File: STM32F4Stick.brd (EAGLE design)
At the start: 44.5 x 23.4 mm, 36 parts, among them U1 MIC5219 3.3V

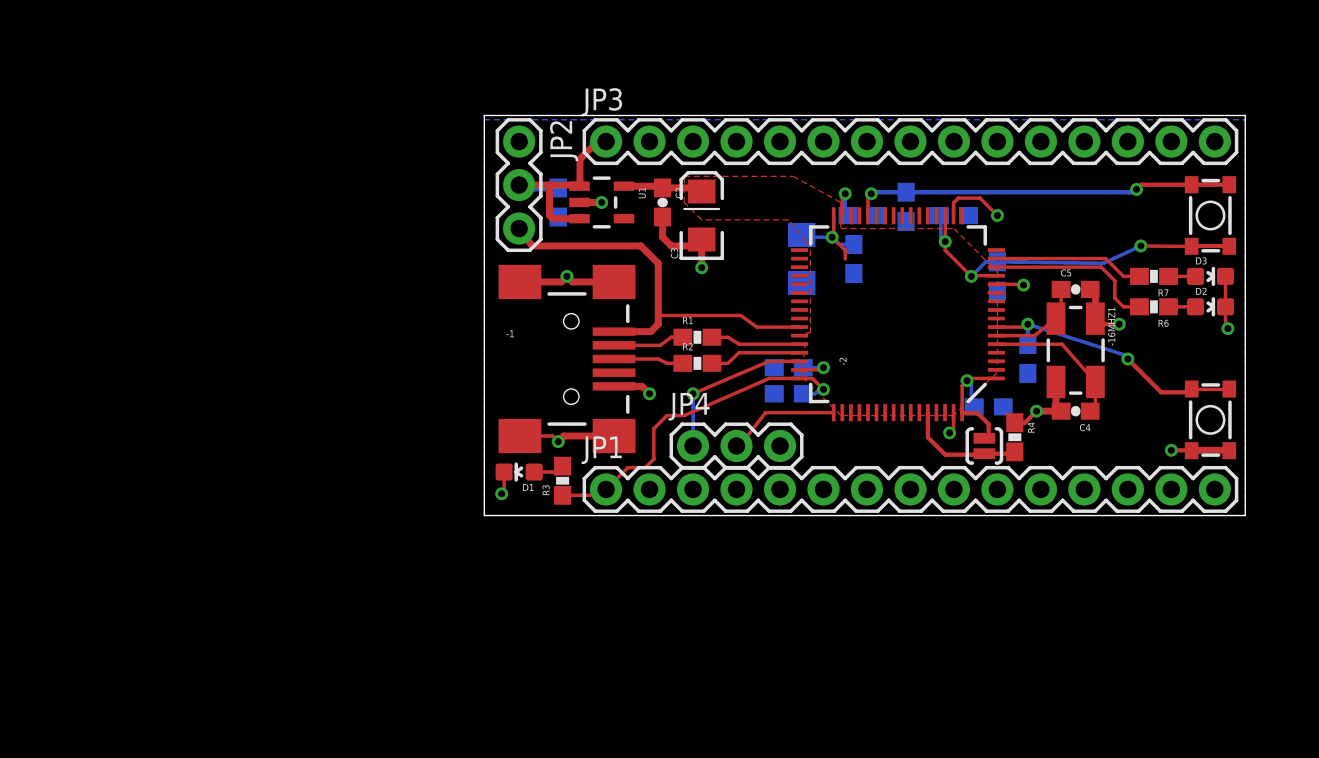
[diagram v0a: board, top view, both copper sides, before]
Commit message: Extension header additions to schematic. Routing is complete on the board. The second extension header connections needs to be added.
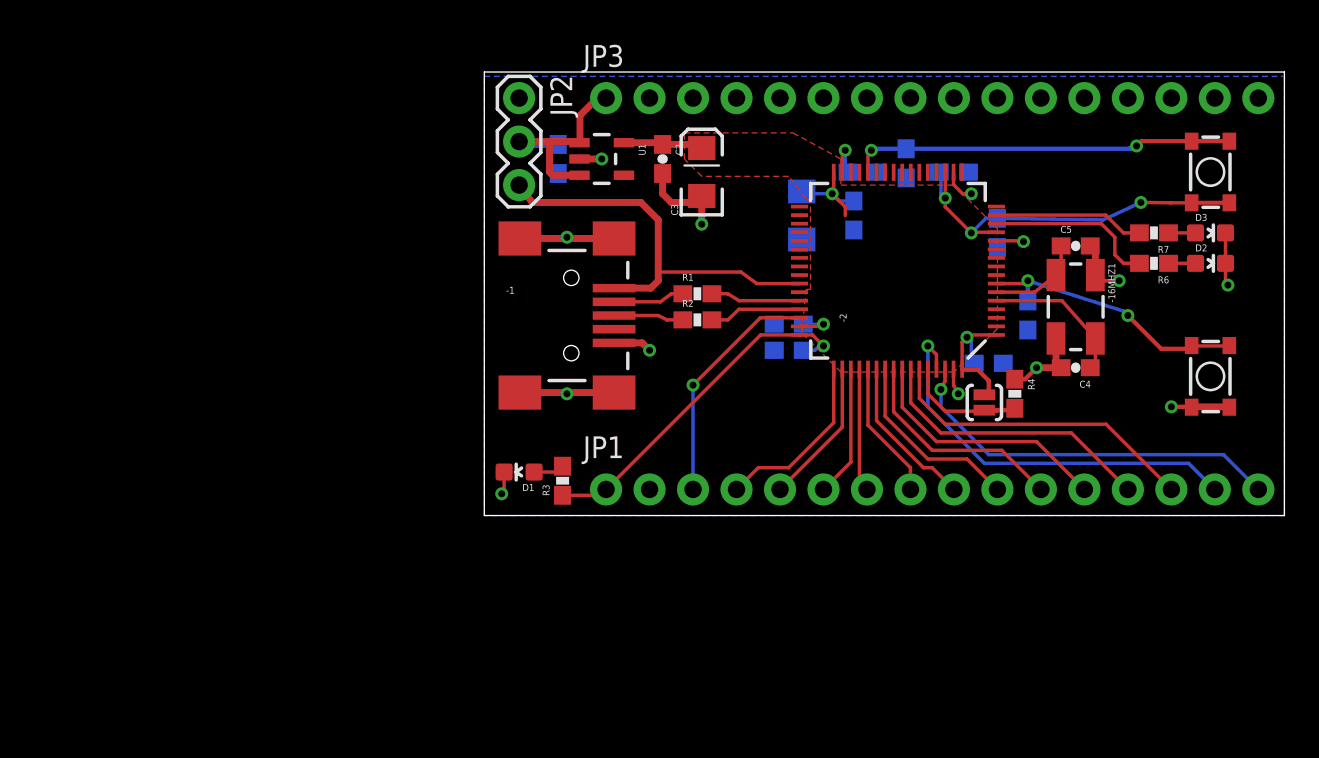
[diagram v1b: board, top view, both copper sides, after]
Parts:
- removed JP4: (no value), SparkFun-Connectors:1X03
- JP1, JP3: value M15 -> M161X16_NO_SILK; device SparkFun-Connectors:1X15 -> SparkFun-Connectors:1X16_NO_SILK
- moved R5 2.54 mm to (24.6, 20.6)
- moved -16MHZ1 2.54 mm to (34.5, 12.2)
- moved -2 2.54 mm to (24.2, 14.3)
- moved C10 2.54 mm to (30.0, 16.5)
- moved C11 2.54 mm to (29.5, 8.89)
- moved C13 2.54 mm to (17.8, 11.2)
- moved D3 2.54 mm to (42.4, 16.5)
- moved R1 2.54 mm to (12.4, 13.0)
- moved R7 2.54 mm to (39.1, 16.5)
- moved R4 2.54 mm to (31.0, 7.11)
- moved S1 2.54 mm to (42.4, 8.13)
- moved SJ1 2.54 mm to (29.2, 6.60)
- moved -1 2.54 mm to (5.08, 11.7)
- moved C1 2.54 mm to (4.32, 20.8)
- moved C12 2.54 mm to (18.5, 17.5)
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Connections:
- removed net N$11: JP1.9
- removed net N$12: JP1.8
- removed net N$13: JP1.7
- removed net N$14: JP1.6
- removed net N$15: JP1.5
- removed net N$16: JP1.4
- removed net N$17: JP1.3
- removed net N$2: JP1.15
- removed net N$5: JP1.14
- removed net N$6: JP1.13
- removed net N$7: JP1.12
- removed net N$8: JP1.11
- removed net N$9: JP1.10
- new net P50: -2.50, JP1.5
- new net P51: -2.51, JP1.6
- new net P52: -2.52, JP1.7
- new net P53: -2.53, JP1.8
- new net P54: -2.54, JP1.9
- new net P55: -2.55, JP1.10
- new net P56: -2.56, JP1.11
- new net P57: -2.57, JP1.12
- new net P58: -2.58, JP1.13
- new net P59: -2.59, JP1.14
- new net P61: -2.61, JP1.15
- new net P62: -2.62, JP1.16
- new net USB_ID: -2.43
- net GND: no longer JP4.3
- net SWDCK: now also JP1.4; no longer JP4.2
- net SWDIO: now also JP1.3; no longer JP4.1
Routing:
- net P61: track 0.00 -> 23.9 mm, vias 0 -> 1
- net P62: track 0.00 -> 22.8 mm, vias 0 -> 1
- net P59: track 0.00 -> 18.6 mm
- net P58: track 0.00 -> 16.7 mm
- net P57: track 0.00 -> 14.9 mm
- net P56: track 0.00 -> 13.0 mm
- net P55: track 0.00 -> 11.1 mm
- net P54: track 0.00 -> 9.19 mm
- net P50: track 0.00 -> 8.53 mm
- net P53: track 0.00 -> 8.05 mm
- net P51: track 0.00 -> 7.69 mm
- net P52: track 0.00 -> 7.21 mm
- net SWDIO: track 9.66 -> 13.9 mm
- net SWDCK: track 7.02 -> 10.4 mm
- net GND: track 43.8 -> 41.9 mm
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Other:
- board size 44.5 x 23.4 mm -> 46.7 x 25.9 mm

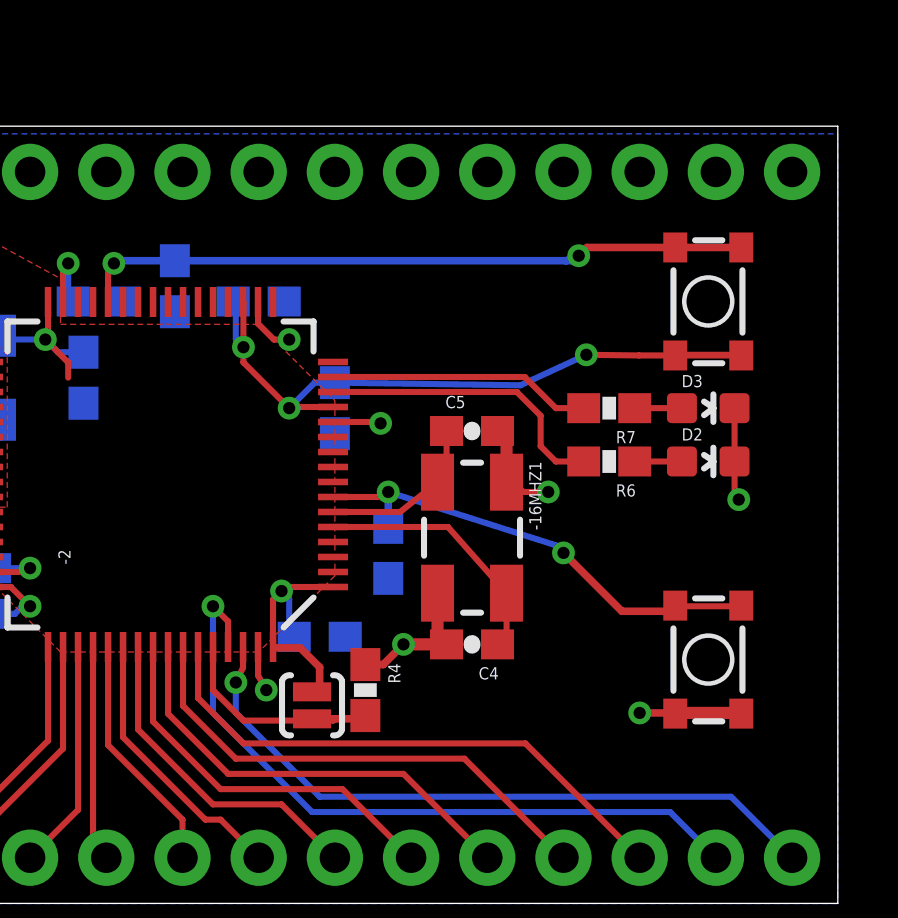
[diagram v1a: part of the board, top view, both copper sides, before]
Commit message: Added SD-Card. Still need to route the extension pins.
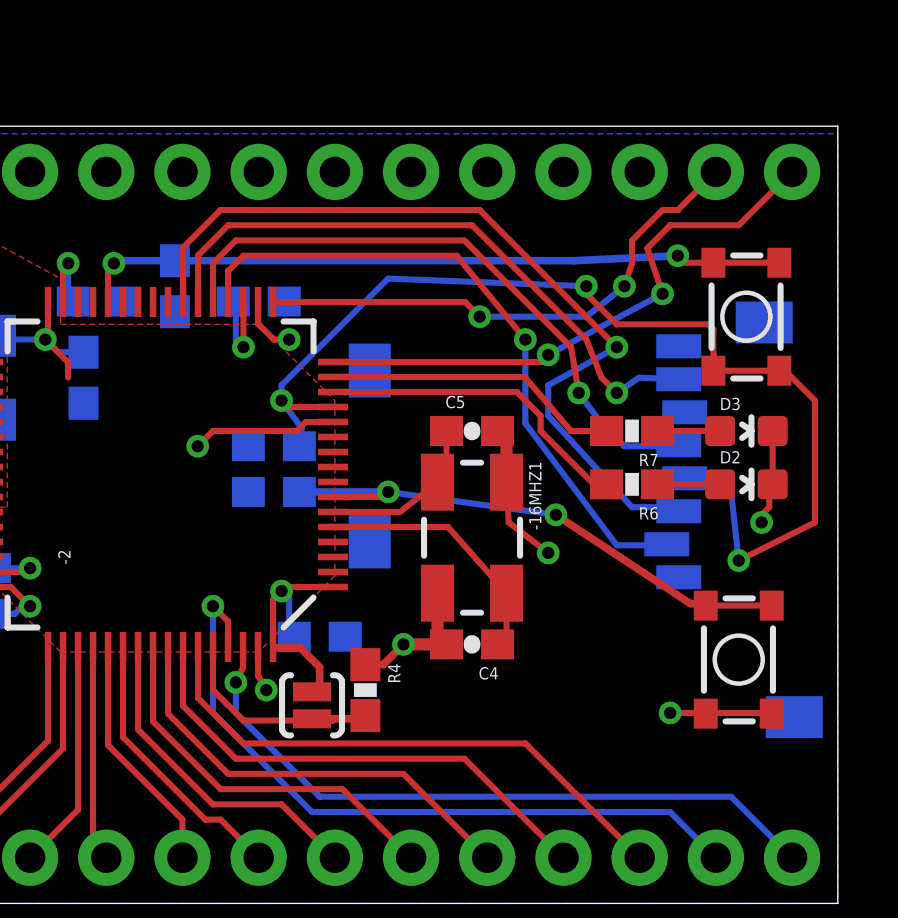
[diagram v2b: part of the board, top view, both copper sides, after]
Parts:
- added U2: USD-SOCKETNEW, SparkFun-Connectors:MICRO-SD-SOCKET-PP
- moved C14 4.32 mm to (27.9, 13.7), turned to 0 degrees
- moved C10 2.40 mm to (27.9, 15.2), turned to 0 degrees
- moved D3 1.48 mm to (43.7, 15.7)
- moved D2 1.48 mm to (43.7, 14.0)
- moved S2 1.37 mm to (43.7, 19.6)
- moved R7 1.08 mm to (39.9, 15.7)
- moved R6 1.08 mm to (39.9, 14.0)
- moved S1 1.02 mm to (43.4, 8.13)
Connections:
- removed net N$20: JP3.15
- new net P16: -2.16, JP3.16
- new net P17: -2.17, JP3.15
- new net SD_CS: -2.20, U2.2
- new net SD_MISO: -2.22, U2.7
- new net SD_MOSI: -2.23, U2.3
- new net SD_SCK: -2.21, U2.5
- net GND: now also U2.6, U2.GND1, U2.GND3
- net VCC: now also U2.4
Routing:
- net SD_MOSI: track 0.00 -> 28.1 mm, vias 0 -> 1
- net SD_CS: track 0.00 -> 22.0 mm, vias 0 -> 1
- net SD_MISO: track 0.00 -> 20.8 mm, vias 0 -> 1
- net SD_SCK: track 0.00 -> 20.7 mm, vias 0 -> 1
- net P16: track 0.00 -> 19.1 mm, vias 0 -> 2
- net P17: track 0.00 -> 17.6 mm, vias 0 -> 2
- net VCC: track 65.3 -> 80.9 mm, vias 6 -> 7
- net GND: track 41.9 -> 47.0 mm
- net NRST: track 16.3 -> 18.6 mm
- net LED_RED: track 8.79 -> 9.94 mm
- net BOOT1: track 23.2 -> 24.0 mm
- net LED_BLUE: track 9.91 -> 10.7 mm
- net N$19: track 1.57 -> 2.08 mm
- net N$18: track 1.57 -> 2.08 mm

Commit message: Finished Schematic / Board layout. Silkscreen needs to be added
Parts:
- removed -16MHZ1: CRYSTAL-GROUNDED, SparkFun-FreqCtrl:CRYSTAL-SMD-5X3
- added Q1: (no value), adafruit:NX3225
- added R10, R11, R8, R9: 100k, SparkFun-Resistors:0603-RES
- moved C7 2.27 mm to (20.6, 15.5)
- moved C3 1.80 mm to (14.5, 19.8), flipped to the bottom
- moved C2 1.52 mm to (11.9, 20.8), flipped to the bottom
- moved C5 1.37 mm to (34.0, 14.5)
- moved R5 1.02 mm to (24.6, 19.6)
- moved U2 1.02 mm to (30.7, 18.8)
- moved C11 1.02 mm to (29.5, 7.87)
- moved -2 1.02 mm to (24.2, 13.3)
- moved C10 1.02 mm to (27.9, 14.2)
- moved C13 1.02 mm to (17.8, 10.2)
- moved C14 1.02 mm to (27.9, 12.7)
- moved C9 1.02 mm to (17.8, 8.64)
- moved D3 1.02 mm to (43.7, 14.7)
- moved R4 1.02 mm to (31.0, 6.10)
- moved R7 1.02 mm to (39.9, 14.7)
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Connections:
- removed net N$21: JP3.14
- removed net N$22: JP3.13
- removed net N$23: JP3.12
- removed net N$24: JP3.11
- removed net N$25: JP3.10
- removed net N$26: JP3.9
- removed net N$27: JP3.8
- removed net N$28: JP3.7
- removed net N$29: JP3.6
- removed net N$30: JP3.5
- removed net N$31: JP3.4
- removed net N$32: JP3.3
- new net P26: -2.26, JP3.14
- new net P27: -2.27, JP3.13
- new net P29: -2.29, JP3.12
- new net P30: -2.30, JP3.11, R9.1
- new net P33: -2.33, JP3.10
- new net P34: -2.34, JP3.9
- new net P35: -2.35, JP3.8
- new net P36: -2.36, JP3.7
- new net P37: -2.37, JP3.6
- new net P39: -2.39, JP3.5
- new net P40: -2.40, JP3.4
- new net P41: -2.41, JP3.3
- net GND: now also Q1.2, Q1.4; no longer -16MHZ1.2, -16MHZ1.4
- net N$3: now also Q1.1; no longer -16MHZ1.3
- net N$4: now also Q1.3; no longer -16MHZ1.1
- net P52: now also R10.1
- net P57: now also R11.1
- net USB_ID: now also R8.1
- net VCC: now also R10.2, R11.2, R8.2, R9.2
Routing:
- net P30: track 0.00 -> 21.9 mm, vias 0 -> 2
- net P26: track 0.00 -> 19.9 mm
- net P27: track 0.00 -> 18.5 mm
- net VCC: track 80.9 -> 98.9 mm, vias 7 -> 9
- net P29: track 0.00 -> 16.7 mm, vias 0 -> 1
- net P33: track 0.00 -> 16.2 mm, vias 0 -> 1
- net P34: track 0.00 -> 15.2 mm
- net P41: track 0.00 -> 14.9 mm
- net P35: track 0.00 -> 14.2 mm
- net P36: track 0.00 -> 13.4 mm
- net P40: track 0.00 -> 13.2 mm
- net P39: track 0.00 -> 12.8 mm
- net P37: track 0.00 -> 12.8 mm
- net GND: track 47.0 -> 41.4 mm, vias 13 -> 18
- net USB_ID: track 0.00 -> 3.18 mm, vias 0 -> 1
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- added copper zone on layer 1, net GND

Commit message: Final version for Rev A.
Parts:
- added C15: 0.1uF, SparkFun-Capacitors:0603-CAP
- added LOGO1: OSHW-LOGOM, SparkFun-Aesthetics:OSHW-LOGO-M
- C5: value 12pF -> 2.2uF
- C6: value 2.2uF -> 12pF
- JP2: device SparkFun-Connectors:1X03 -> SparkFun-Connectors:1X03_NO_SILK
- R10, R11: value 100k -> 1K
- R4, R5: value 10K -> 100k
- R6, R7: value 1K -> 100k
- R8, R9: value 100k -> 10K
- moved R7 21.2 mm to (21.8, 3.56), flipped to the bottom, turned to 0 degrees
- moved R10 20.5 mm to (39.9, 13.2), flipped to the top, turned to 180 degrees
- moved R11 20.5 mm to (39.9, 14.7), flipped to the top, turned to 180 degrees
- moved R6 19.8 mm to (21.8, 5.08), flipped to the bottom, turned to 0 degrees
- moved R5 14.4 mm to (38.9, 21.6), turned to 180 degrees
- moved R9 14.4 mm to (24.6, 19.6), turned to 90 degrees
- moved C5 12.8 mm to (22.1, 19.1), flipped to the bottom, turned to 180 degrees
- moved C6 12.8 mm to (34.0, 14.5), flipped to the top, turned to 0 degrees
- moved R4 10.7 mm to (21.1, 10.2), flipped to the bottom
- moved R8 10.7 mm to (31.0, 6.10), flipped to the top
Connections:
- new net N$2: C15.1, U1.4
- net BOOT0: now also R8.2; no longer R4.2
- net BOOT1: now also R9.2; no longer R5.2
- net GND: now also C15.2, R8.1, R9.1; no longer R4.1, R5.1
- net LED_BLUE: now also R10.2; no longer R6.2
- net LED_RED: now also R11.2; no longer R7.2
- net N$1: now also C5.1; no longer C6.1
- net N$18: now also R10.1; no longer R6.1
- net N$19: now also R11.1; no longer R7.1
- net N$4: now also C6.1; no longer C5.1
- net P30: now also R5.1; no longer R9.1
- net P52: now also R7.1; no longer R10.1
- net P57: now also R6.1; no longer R11.1
- net USB_ID: now also R4.1; no longer R8.1
- net VCC: now also R4.2, R5.2, R6.2, R7.2; no longer R10.2, R11.2, R8.2, R9.2
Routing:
- net N$2: track 0.00 -> 2.36 mm
- net GND: track 41.4 -> 40.9 mm
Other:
- board text added: "100k"
- board text added: "3V3"
- board text added: "5V"
- board text added: "A13"
- board text added: "A14"
- board text added: "A15"
- board text added: "A2"
- board text added: "A3"
- board text added: "A8"
- board text added: "B0"
- board text added: "B1"
- board text added: "B10"
- board text added: "B11"
- board text added: "B12"
- board text added: "B13"
- board text added: "B14"
- board text added: "B15"
- board text added: "B3"
- board text added: "B4"
- board text added: "B5"
- board text added: "B6"
- board text added: "B7"
- board text added: "B8"
- board text added: "B9"
- board text added: "BOOT0"
- board text added: "BOOT1/PB2"
- board text added: "BTN"
- board text added: "C10"
- board text added: "C11"
- board text added: "C12"
- board text added: "C6"
- board text added: "C8"
- board text added: "C9"
- board text added: "D2"
- board text added: "FURKAN CAYCI"
- board text added: "GND"
- board text added: "JTCK"
- board text added: "JTD0"
- board text added: "JTDI"
- board text added: "JTMS"
- board text added: "JUNE 2014"
- board text added: "LED1"
- board text added: "LED2"
- board text added: "MISO"
- board text added: "MOSI"
- board text added: "NJTRST"
- board text added: "NSS"
- board text added: "PA0"
- board text added: "PA1"
- board text added: "POWER"
- board text added: "RESET"
- board text added: "REV A"
- board text added: "RX UART2 TX"
- board text added: "SCK"
- board text added: "SCL I2C3 SDA"
- board text added: "SD/MMC CARD (SPI MODE) SPI1 A4,5,6,7"
- board text added: "SDA I2C2 SCL"
- board text added: "SPI2"
- board text added: "STM32F4Stick"
- board text added: "SWCLK"
- board text added: "SWD"
- board text added: "SWDIO"
- board text added: "USB"
- board text added: "USB ID Pull high"
- board text added: "https://github.com/fcayci/STM32F4Stick"

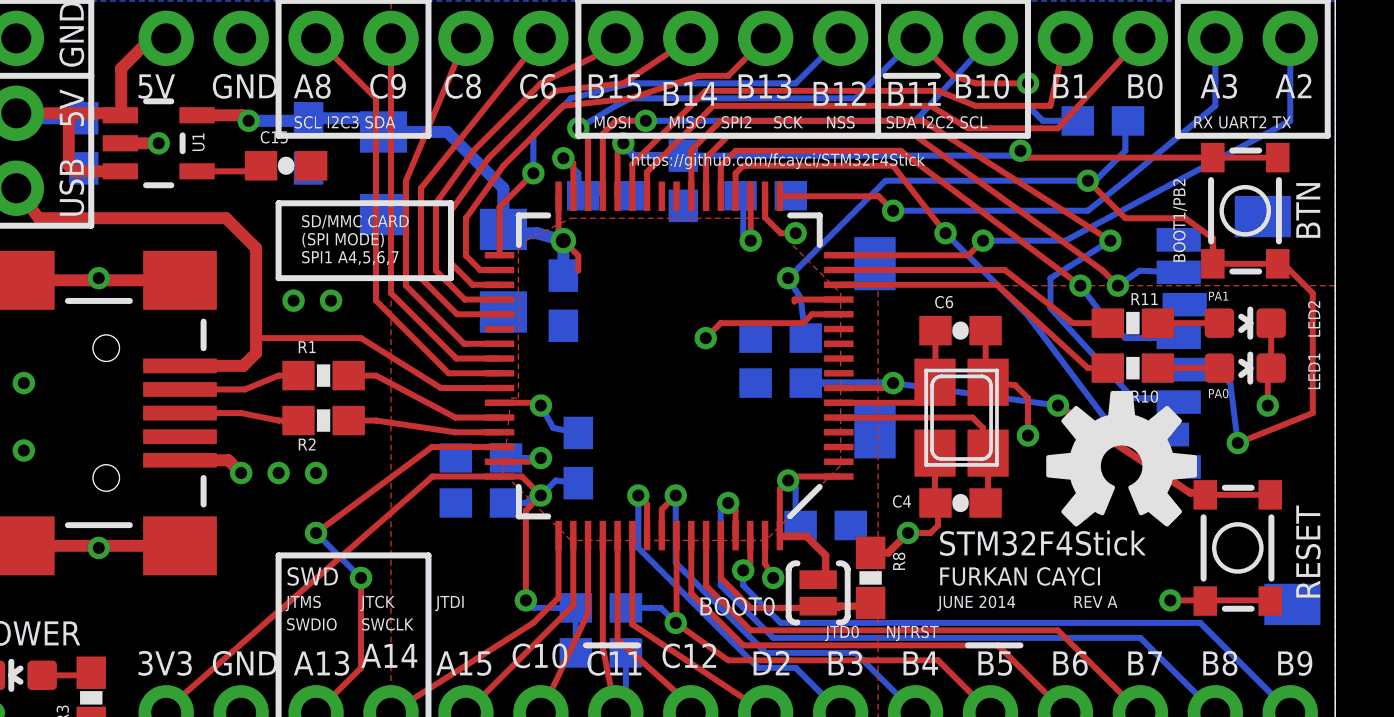
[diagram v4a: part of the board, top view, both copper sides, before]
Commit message: Small fixes to the usb resistors and a component might get in the way of SD card slot.
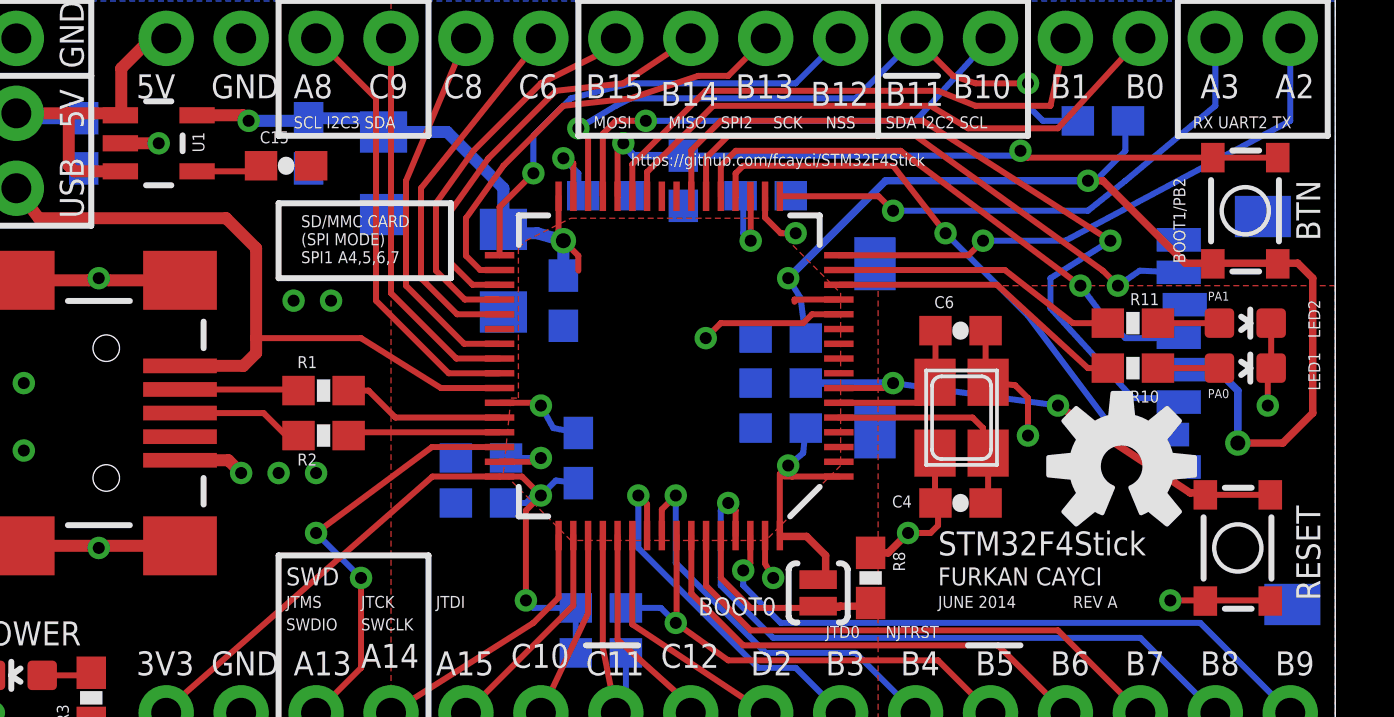
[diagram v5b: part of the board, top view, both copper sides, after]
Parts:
- moved C11 3.64 mm to (27.9, 11.2), turned to 0 degrees
- moved R1 0.51 mm to (12.4, 12.4)
- moved R2 0.51 mm to (12.4, 10.9)
